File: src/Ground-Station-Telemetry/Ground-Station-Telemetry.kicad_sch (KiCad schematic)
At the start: 34 parts, among them J1 Jumper_NO, P1 3220-20-0200-00, U1 STM32H750VBTx, U2 LMS8117AMP-3.3_NOPB, Y1 ECS-240-18-33-JGN-TR

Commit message: routed rev1
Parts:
- added D2: SML-LX1206GC-TR, Ground-Station-Telemetry:SML-LX1206GC-TR, symbol Ground-Station-Telemetry:SML-LX1206GC-TR
- added R6: 240, Ground-Station-Telemetry:RES_0603, symbol Ground-Station-Telemetry:RES_0603
- H1, H2, H3, H4: footprint (none) -> Engine-Controller:MountingHole_4.3mm_M4_DIN965
- J1: footprint (none) -> Engine-Controller:RES_0603
- renumbered C6 to C5, C7 to C6, C5 to C7, D2 to D3, R6 to R7
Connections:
- net 5V: now also D2.2
- net Earth: now also R6.1
- net LORA_IO0: now also U1.30 (PA6); no longer U1.81 (PD0)
- net LORA_IO1: now also U1.31 (PA7); no longer U1.82 (PD1)
- net LORA_IO2: now also U1.32 (PC4); no longer U1.83 (PD2)
- net LORA_IO3: now also U1.28 (PA4); no longer U1.84 (PD3)
- net LORA_IO4: now also U1.29 (PA5); no longer U1.85 (PD4)
- net LORA_IO5: now also U1.15 (PC0); no longer U1.86 (PD5)
- net LORA_RST: now also U1.24 (PA2); no longer U1.47 (PB11)
- net LORA_SS: now also U1.25 (PA3); no longer U1.51 (PB12)
- net STATUS_B: now also U1.41 (PE11); no longer U1.42 (PE12)
- net STATUS_G: now also U1.42 (PE12); no longer U1.41 (PE11)
- net XBEE_DIO1: now also U1.87 (PD6); no longer U1.55 (PD8)
- net XBEE_DIO5: now also U1.84 (PD3); no longer U1.56 (PD9)
- net XBEE_DIO6: now also U1.85 (PD4); no longer U1.57 (PD10)
- net XBEE_DIO7: now also U1.82 (PD1); no longer U1.58 (PD11)
- net XBEE_DIO8: now also U1.8 (PC14); no longer U1.59 (PD12)
- net XBEE_SS: now also U1.86 (PD5); no longer U1.36 (PB2)
- net ~{XBEE_RST}: now also U1.7 (PC13); no longer U1.87 (PD6)
- net ~{XBEE_SLEEP}: now also U1.83 (PD2); no longer U1.60 (PD13)
- new net: D2.1, R6.2
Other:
- note added: "5V Supply Indication"
- moved on the sheet: C4, C7, D3, R7, U2

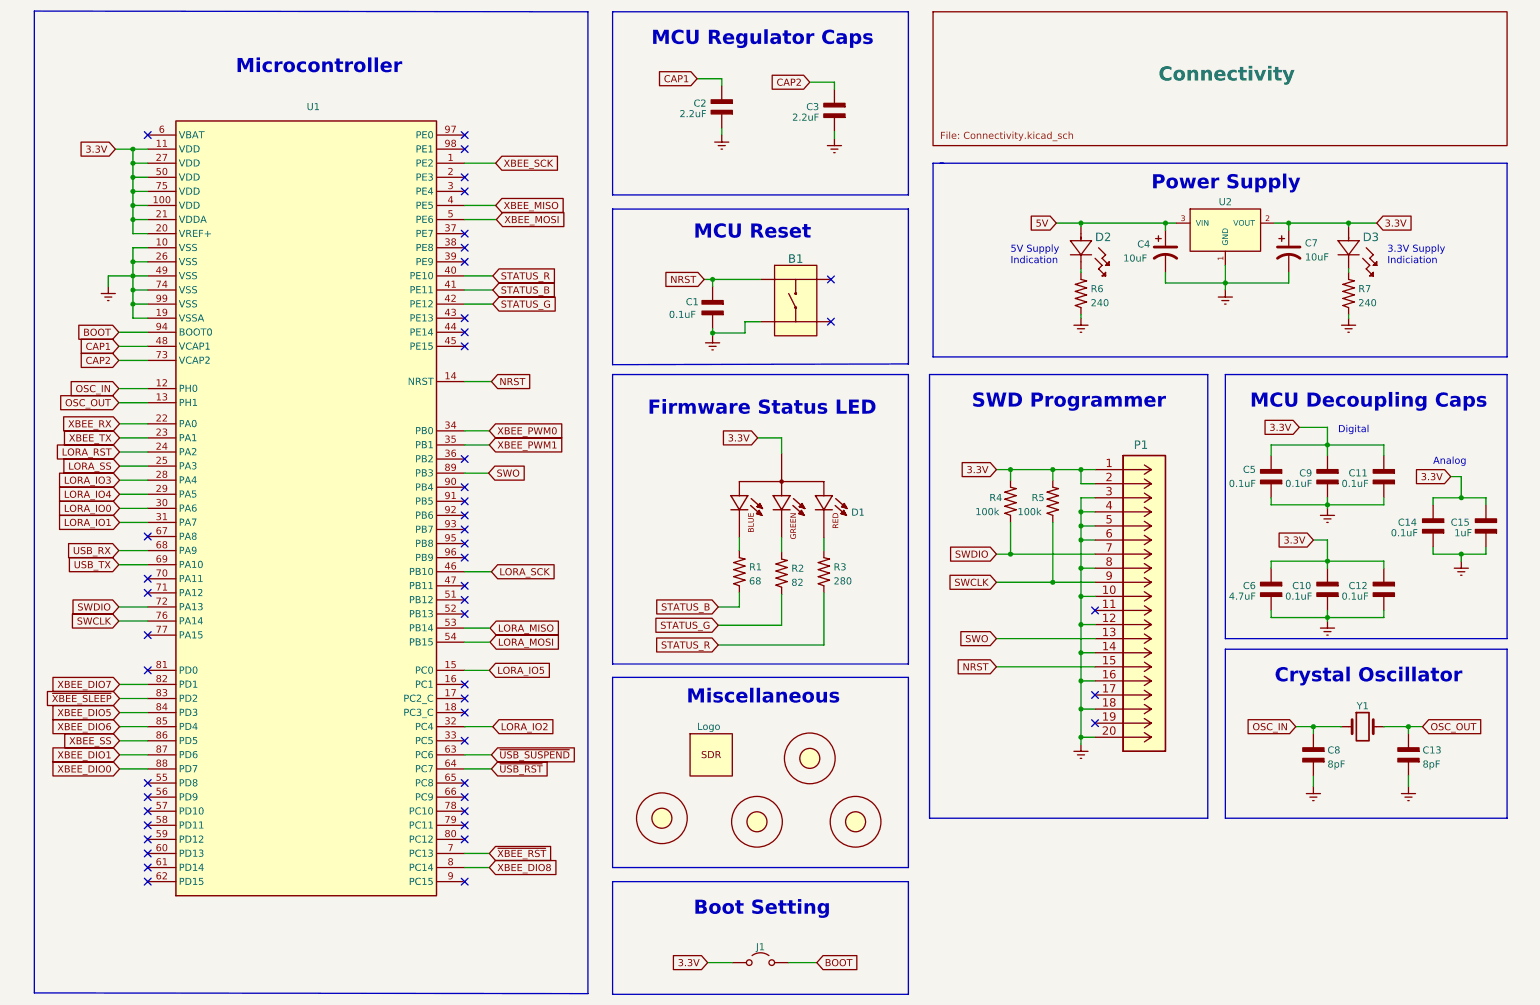
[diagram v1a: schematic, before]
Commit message: added RS485 transceiver to schematic
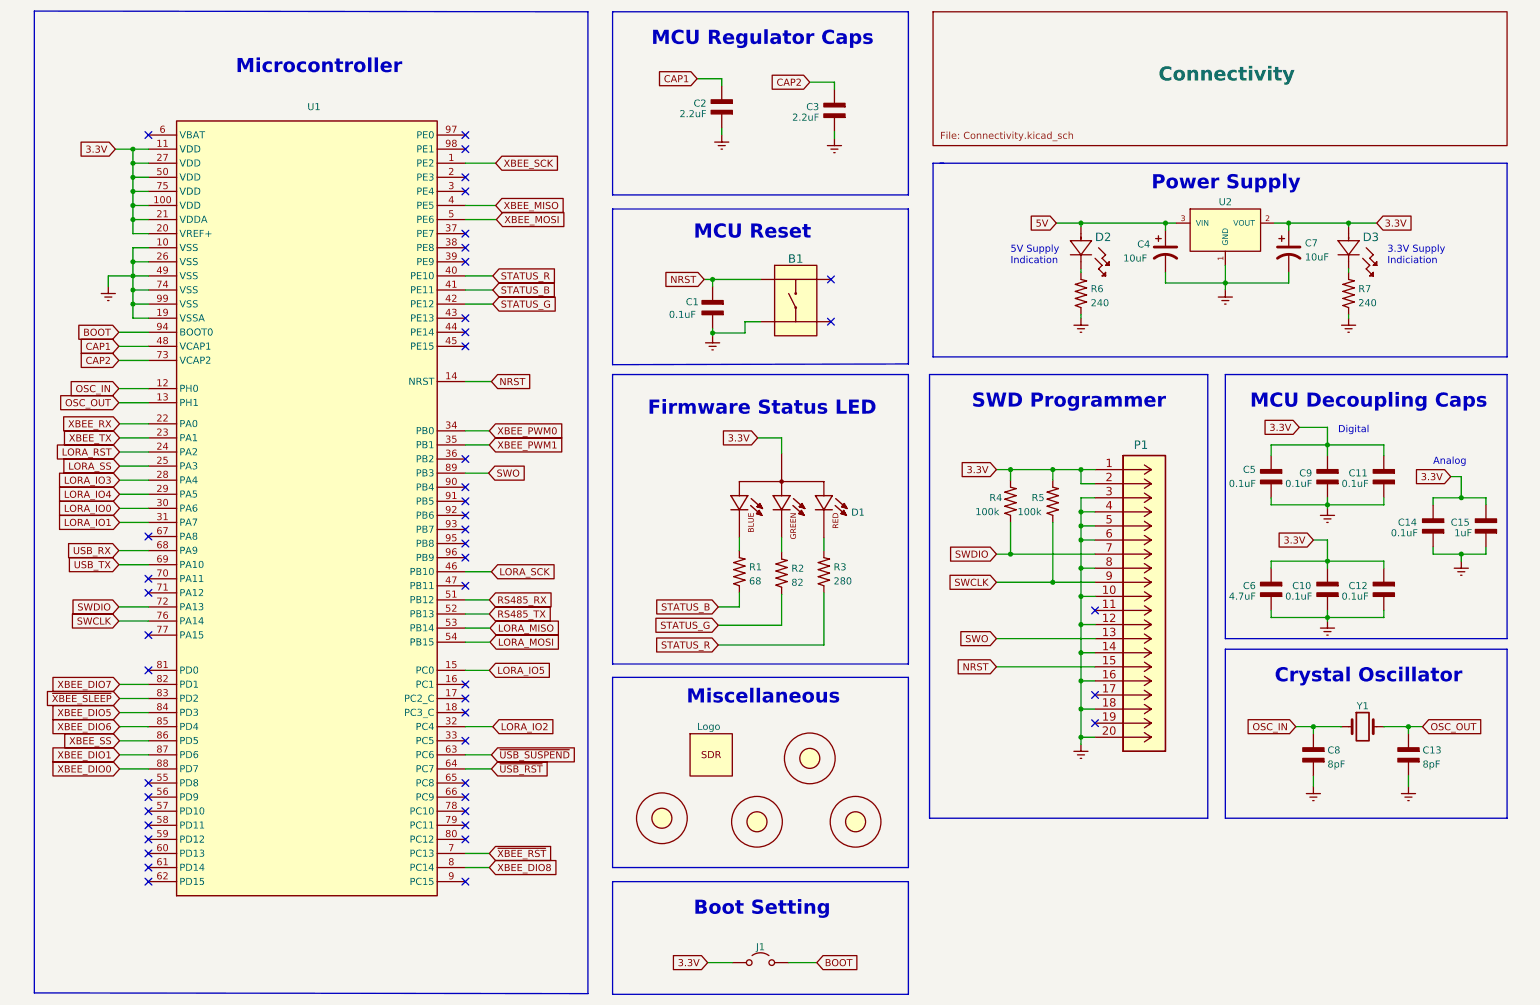
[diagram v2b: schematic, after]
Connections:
- net RS485_RX: now reaches U1.51 (PB12)
- net RS485_TX: now reaches U1.52 (PB13)
- no-connect marks 49 -> 47

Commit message: finished initial rev 2 routing
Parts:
- removed H3: Mounting-Hole, Engine-Controller:MountingHole_4.3mm_M4_DIN965, symbol Ground-Station-Telemetry:Mounting-Hole
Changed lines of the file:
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@@
-    )
-  )
-  (symbol (lib_id "Ground-Station-Telemetry:Mounting-Hole") (at 156.845 150.495 0) (unit 1)
-    (in_bom yes) (on_board yes) (dnp no) (fields_autoplaced)
-    (property "Reference" "H3" (at 156.845 144.145 0)
-      (effects (font (size 1.27 1.27)) hide)
-    )
-    (property "Value" "Mounting-Hole" (at 156.845 155.575 0)
-      (effects (font (size 1.27 1.27)) hide)
-    )
-    (property "Footprint" "Engine-Controller:MountingHole_4.3mm_M4_DIN965" (at 156.845 150.495 0)
-      (effects (font (size 1.27 1.27)) hide)
-    )
-    (property "Datasheet" "" (at 156.845 150.495 0)
-      (effects (font (size 1.27 1.27)) hide)
-    )
-    (instances
-      (project "Ground-Station-Telemetry"
-        (path "/8e3fff47-8adf-433e-a9ef-a2ec6a2108a7"
-          (reference "H3") (unit 1)
-        )
-      )
     )
   )
@@
     )
   )
-  (symbol (lib_id "Ground-Station-Telemetry:Mounting-Hole") (at 165.1 161.925 0) (unit 1)
-    (in_bom yes) (on_board yes) (dnp no) (fields_autoplaced)
-    (property "Reference" "H4" (at 165.1 155.575 0)
-      (effects (font (size 1.27 1.27)) hide)
-    )
-    (property "Value" "Mounting-Hole" (at 165.1 167.005 0)
-      (effects (font (size 1.27 1.27)) hide)
-    )
-    (property "Footprint" "Engine-Controller:MountingHole_4.3mm_M4_DIN965" (at 165.1 161.925 0)
-      (effects (font (size 1.27 1.27)) hide)
-    )
-    (property "Datasheet" "" (at 165.1 161.925 0)
+  (symbol (lib_id "Ground-Station-Telemetry:Mounting-Hole") (at 157.988 149.606 0) (unit 1)
+    (in_bom yes) (on_board yes) (dnp no) (fields_autoplaced)
+    (property "Reference" "H4" (at 157.988 143.256 0)
+      (effects (font (size 1.27 1.27)) hide)
+    )
+    (property "Value" "Mounting-Hole" (at 157.988 154.686 0)
+      (effects (font (size 1.27 1.27)) hide)
+    )
+    (property "Footprint" "Engine-Controller:MountingHole_4.3mm_M4_DIN965" (at 157.988 149.606 0)
+      (effects (font (size 1.27 1.27)) hide)
+    )
+    (property "Datasheet" "" (at 157.988 149.606 0)
       (effects (font (size 1.27 1.27)) hide)
     )
@@
     )
   )
-  (symbol (lib_id "Ground-Station-Telemetry:Mounting-Hole") (at 130.175 161.29 0) (unit 1)
-    (in_bom yes) (on_board yes) (dnp no) (fields_autoplaced)
-    (property "Reference" "H1" (at 130.175 154.94 0)
-      (effects (font (size 1.27 1.27)) hide)
-    )
-    (property "Value" "Mounting-Hole" (at 130.175 166.37 0)
-      (effects (font (size 1.27 1.27)) hide)
-    )
-    (property "Footprint" "Engine-Controller:MountingHole_4.3mm_M4_DIN965" (at 130.175 161.29 0)
-      (effects (font (size 1.27 1.27)) hide)
-    )
-    (property "Datasheet" "" (at 130.175 161.29 0)
+  (symbol (lib_id "Ground-Station-Telemetry:Mounting-Hole") (at 138.684 161.29 0) (unit 1)
+    (in_bom yes) (on_board yes) (dnp no) (fields_autoplaced)
+    (property "Reference" "H1" (at 138.684 154.94 0)
+      (effects (font (size 1.27 1.27)) hide)
+    )
+    (property "Value" "Mounting-Hole" (at 138.684 166.37 0)
+      (effects (font (size 1.27 1.27)) hide)
+    )
+    (property "Footprint" "Engine-Controller:MountingHole_4.3mm_M4_DIN965" (at 138.684 161.29 0)
+      (effects (font (size 1.27 1.27)) hide)
+    )
+    (property "Datasheet" "" (at 138.684 161.29 0)
       (effects (font (size 1.27 1.27)) hide)
     )
@@
     )
   )
-  (symbol (lib_id "Ground-Station-Telemetry:Mounting-Hole") (at 147.32 161.925 0) (unit 1)
-    (in_bom yes) (on_board yes) (dnp no) (fields_autoplaced)
-    (property "Reference" "H2" (at 147.32 155.575 0)
-      (effects (font (size 1.27 1.27)) hide)
-    )
-    (property "Value" "Mounting-Hole" (at 147.32 167.005 0)
-      (effects (font (size 1.27 1.27)) hide)
-    )
-    (property "Footprint" "Engine-Controller:MountingHole_4.3mm_M4_DIN965" (at 147.32 161.925 0)
-      (effects (font (size 1.27 1.27)) hide)
-    )
-    (property "Datasheet" "" (at 147.32 161.925 0)
-      (effects (font (size 1.27 1.27)) hide)
-    )
+  (symbol (lib_id "Ground-Station-Telemetry:Mounting-Hole") (at 157.734 162.052 0) (unit 1)
+    (in_bom yes) (on_board yes) (dnp no) (fields_autoplaced)
+    (property "Reference" "H2" (at 157.734 155.702 0)
+      (effects (font (size 1.27 1.27)) hide)
+    )
+    (property "Value" "Mounting-Hole" (at 157.734 167.132 0)
+      (effects (font (size 1.27 1.27)) hide)
+    )
+    (property "Footprint" "Engine-Controller:MountingHole_4.3mm_M4_DIN965" (at 157.734 162.052 0)
+      (effects (font (size 1.27 1.27)) hide)
+    )
+    (property "Datasheet" "" (at 157.734 162.052 0)
+      (effects (font (size 1.27 1.27)) hide)
+    )
